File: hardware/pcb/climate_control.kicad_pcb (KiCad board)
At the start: 2 copper layers, 18 x 60 mm, 43 parts, among them J1 Switch, J2 BatteryIn, J3 USB_C, J4 HeatElement, J5 ICSP, Q1 NTR3C21NZ, Q2 NTR3C21NZ, U1 TP4056, U2 XB8089A, U3 ATmega328PB-AU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

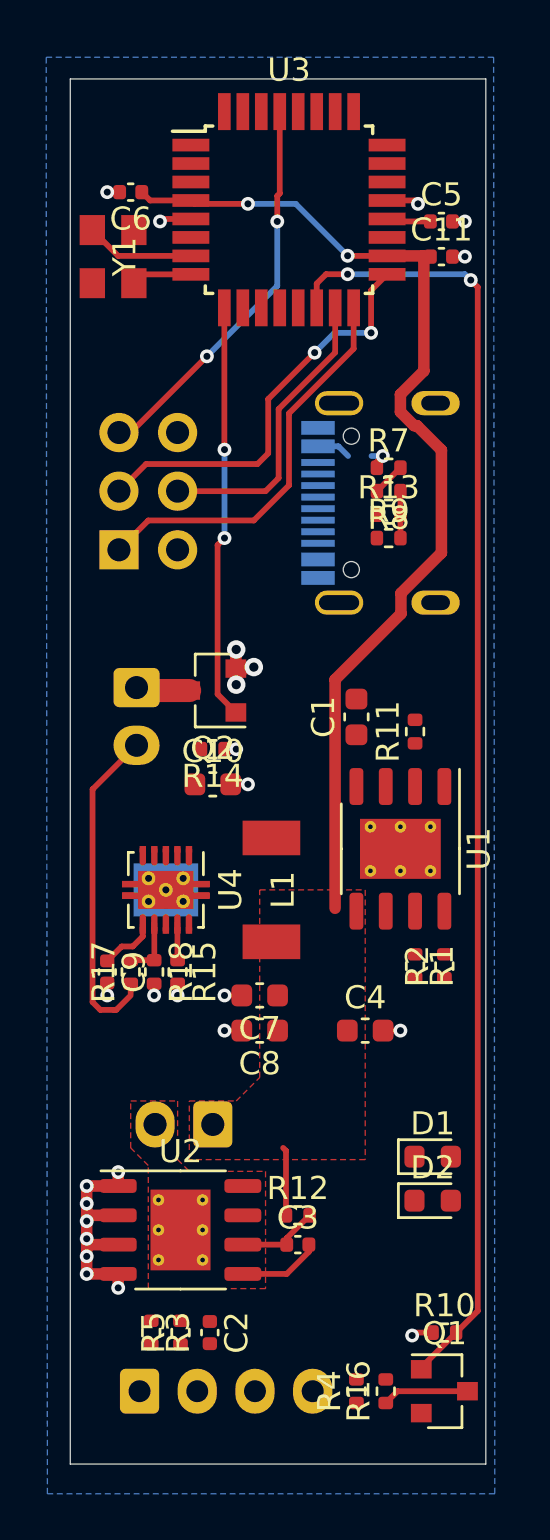
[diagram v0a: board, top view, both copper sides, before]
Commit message: Removed resistor on TP4056.
Updated on PCB the routing.
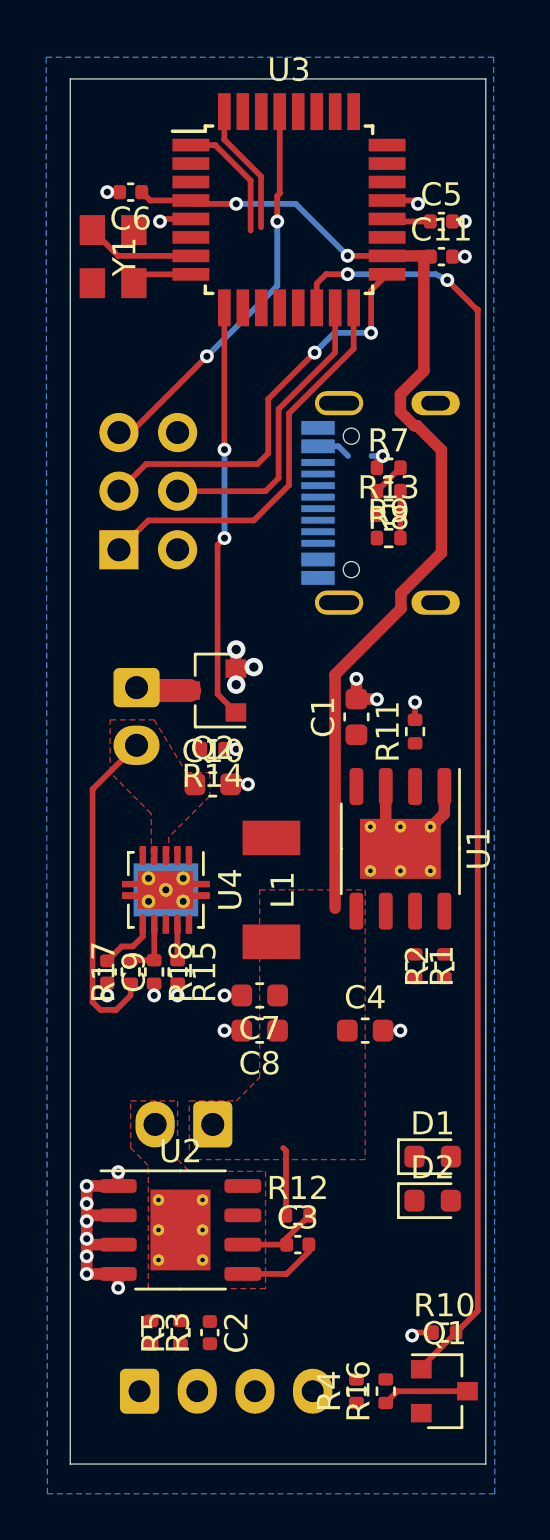
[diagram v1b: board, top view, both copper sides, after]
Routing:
- net GND: track 25.2 -> 34.4 mm, vias 25 -> 28
- net SWITCH: track 0.00 -> 5.67 mm
- net BOOST_EN: track 1.57 -> 6.96 mm
- net LED: track 56.4 -> 55.8 mm
- added copper zone on F.Cu, net +VSW
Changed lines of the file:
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@@
     (thickness 1.6)
     (drawings 4)
-    (tracks 184)
+    (tracks 203)
     (zones 0)
     (modules 43)
@@
   (segment (start 110.335 150.805) (end 109.375 151.765) (width 0.25) (layer F.Cu) (net 1))
   (segment (start 110.335 150.495) (end 110.335 150.805) (width 0.25) (layer F.Cu) (net 1))
+  (segment (start 106.674 102.62759) (end 108.263011 104.216601) (width 0.25) (layer F.Cu) (net 3))
+  (segment (start 106.674 101.414) (end 106.674 102.62759) (width 0.25) (layer F.Cu) (net 3))
+  (segment (start 108.263011 104.216601) (end 108.263011 106.426) (width 0.25) (layer F.Cu) (net 3))
   (segment (start 107.475 150.495) (end 109.375 150.495) (width 0.25) (layer F.Cu) (net 4))
   (segment (start 109.375 150.215) (end 110.365 149.225) (width 0.25) (layer F.Cu) (net 4))
@@
   (via (at 112.014 107.657997) (size 0.6) (drill 0.3) (layers F.Cu B.Cu) (net 5))
   (segment (start 112.020003 107.664) (end 112.014 107.657997) (width 0.25) (layer F.Cu) (net 5))
-  (via (at 107.696 105.41) (size 0.6) (drill 0.3) (layers F.Cu B.Cu) (net 5))
-  (segment (start 112.014 107.657997) (end 109.766003 105.41) (width 0.25) (layer B.Cu) (net 5))
-  (segment (start 109.766003 105.41) (end 107.696 105.41) (width 0.25) (layer B.Cu) (net 5))
-  (segment (start 105.37 105.41) (end 105.224 105.264) (width 0.25) (layer F.Cu) (net 5))
-  (segment (start 107.696 105.41) (end 105.37 105.41) (width 0.25) (layer F.Cu) (net 5))
   (segment (start 109.345 149.225) (end 109.345 146.429) (width 0.25) (layer F.Cu) (net 5))
   (segment (start 109.345 146.429) (end 109.22 146.304) (width 0.25) (layer F.Cu) (net 5))
@@
   (segment (start 103.458 105.264) (end 103.096 104.902) (width 0.25) (layer F.Cu) (net 5))
   (segment (start 105.224 105.264) (end 103.458 105.264) (width 0.25) (layer F.Cu) (net 5))
-  (segment (start 114.32399 123.16601) (end 111.46999 126.02001) (width 0.5) (layer F.Cu) (net 5))
   (segment (start 116.078 116.078) (end 116.078 120.526128) (width 0.5) (layer F.Cu) (net 5))
   (segment (start 116.078 120.526128) (end 114.32399 122.280138) (width 0.5) (layer F.Cu) (net 5))
-  (segment (start 111.46999 126.02001) (end 111.46999 135.92601) (width 0.5) (layer F.Cu) (net 5))
   (segment (start 115.284 107.758002) (end 115.316 107.790002) (width 0.5) (layer F.Cu) (net 5))
   (segment (start 115.284 107.664) (end 115.284 107.758002) (width 0.5) (layer F.Cu) (net 5))
   (segment (start 115.316 107.790002) (end 115.316 112.648128) (width 0.5) (layer F.Cu) (net 5))
-  (segment (start 114.32399 122.280138) (end 114.32399 123.16601) (width 0.5) (layer F.Cu) (net 5))
   (segment (start 115.316 112.648128) (end 114.3 113.664128) (width 0.5) (layer F.Cu) (net 5))
   (segment (start 114.3 114.423872) (end 114.3 113.664128) (width 0.5) (layer F.Cu) (net 5))
@@
   (segment (start 115.01901 115.01901) (end 114.895138 115.01901) (width 0.5) (layer F.Cu) (net 5))
   (segment (start 116.078 116.078) (end 115.01901 115.01901) (width 0.5) (layer F.Cu) (net 5))
+  (segment (start 105.37 105.41) (end 105.224 105.264) (width 0.25) (layer F.Cu) (net 5))
+  (segment (start 107.188 105.41) (end 105.37 105.41) (width 0.25) (layer F.Cu) (net 5))
+  (segment (start 109.766003 105.41) (end 112.014 107.657997) (width 0.25) (layer B.Cu) (net 5))
+  (via (at 107.188 105.41) (size 0.6) (drill 0.3) (layers F.Cu B.Cu) (net 5))
+  (segment (start 107.188 105.41) (end 109.766003 105.41) (width 0.25) (layer B.Cu) (net 5))
+  (segment (start 114.32399 122.945008) (end 114.32399 122.280138) (width 0.5) (layer F.Cu) (net 5))
+  (segment (start 111.46999 125.799008) (end 114.32399 122.945008) (width 0.5) (layer F.Cu) (net 5))
+  (segment (start 111.46999 135.92601) (end 111.46999 125.799008) (width 0.5) (layer F.Cu) (net 5))
   (segment (start 113.832 106.172) (end 113.724 106.064) (width 0.25) (layer F.Cu) (net 6))
   (segment (start 115.598 106.172) (end 113.832 106.172) (width 0.25) (layer F.Cu) (net 6))
@@
   (segment (start 110.674 109.914) (end 110.674 108.864) (width 0.25) (layer F.Cu) (net 15))
   (segment (start 110.674 108.864) (end 111.08 108.458) (width 0.25) (layer F.Cu) (net 15))
-  (via (at 117.348 108.712) (size 0.6) (drill 0.3) (layers F.Cu B.Cu) (net 15))
-  (segment (start 112.014 108.458) (end 117.094 108.458) (width 0.25) (layer B.Cu) (net 15))
-  (segment (start 117.094 108.458) (end 117.348 108.712) (width 0.25) (layer B.Cu) (net 15))
-  (segment (start 117.64999 153.37001) (end 116.715 154.305) (width 0.25) (layer F.Cu) (net 15))
-  (segment (start 117.348 108.712) (end 117.64999 109.01399) (width 0.25) (layer F.Cu) (net 15))
-  (segment (start 117.64999 109.01399) (end 117.64999 153.37001) (width 0.25) (layer F.Cu) (net 15))
   (segment (start 115.205 155.815) (end 116.715 154.305) (width 0.25) (layer F.Cu) (net 15))
   (segment (start 115.205 155.895) (end 115.205 155.815) (width 0.25) (layer F.Cu) (net 15))
+  (via (at 116.332 108.712) (size 0.6) (drill 0.3) (layers F.Cu B.Cu) (net 15))
+  (segment (start 115.824 108.458) (end 112.014 108.458) (width 0.25) (layer B.Cu) (net 15))
+  (segment (start 116.332 108.712) (end 115.824 108.458) (width 0.25) (layer B.Cu) (net 15))
+  (segment (start 117.64999 153.37001) (end 116.715 154.305) (width 0.25) (layer F.Cu) (net 15))
+  (segment (start 117.64999 109.982) (end 117.64999 153.37001) (width 0.25) (layer F.Cu) (net 15))
+  (segment (start 117.602 109.982) (end 116.332 108.712) (width 0.25) (layer F.Cu) (net 15))
+  (segment (start 117.64999 109.982) (end 117.602 109.982) (width 0.25) (layer F.Cu) (net 15))
   (via (at 106.68 116.055999) (size 0.6) (drill 0.3) (layers F.Cu B.Cu) (net 18))
   (segment (start 106.674 109.914) (end 106.674 116.049999) (width 0.25) (layer F.Cu) (net 18))
@@
   (segment (start 104.64 138.166) (end 104.648 138.174) (width 0.25) (layer F.Cu) (net 19))
   (segment (start 104.64 136.603) (end 104.64 138.166) (width 0.25) (layer F.Cu) (net 19))
+  (segment (start 107.813001 104.403001) (end 107.813001 106.562999) (width 0.25) (layer F.Cu) (net 19))
+  (segment (start 105.224 102.864) (end 106.274 102.864) (width 0.25) (layer F.Cu) (net 19))
+  (segment (start 106.274 102.864) (end 107.813001 104.403001) (width 0.25) (layer F.Cu) (net 19))
   (segment (start 103.64 138.166) (end 103.632 138.174) (width 0.25) (layer F.Cu) (net 21))
   (segment (start 103.64 136.603) (end 103.64 138.166) (width 0.25) (layer F.Cu) (net 21))
@@
   (segment (start 102.136 104.902) (end 101.6 104.902) (width 0.25) (layer F.Cu) (net 56))
   (segment (start 114.302 117.856) (end 114.302 119.888) (width 0.25) (layer F.Cu) (net 56))
+  (segment (start 113.665 132.715) (end 114.3 133.35) (width 0.5) (layer F.Cu) (net 56))
+  (segment (start 113.665 130.65) (end 113.665 132.715) (width 0.5) (layer F.Cu) (net 56))
+  (segment (start 116.205 130.65) (end 116.205 131.826) (width 0.5) (layer F.Cu) (net 56))
+  (segment (start 114.681 133.35) (end 114.3 133.35) (width 0.5) (layer F.Cu) (net 56))
+  (segment (start 116.205 131.826) (end 114.681 133.35) (width 0.5) (layer F.Cu) (net 56))
+  (via (at 114.935 127) (size 0.6) (drill 0.3) (layers F.Cu B.Cu) (net 56))
+  (segment (start 114.935 127.76) (end 114.935 127) (width 0.25) (layer F.Cu) (net 56))
+  (via (at 113.284 126.873) (size 0.6) (drill 0.3) (layers F.Cu B.Cu) (net 56))
+  (segment (start 112.395 126.86) (end 113.271 126.86) (width 0.5) (layer F.Cu) (net 56))
+  (segment (start 113.271 126.86) (end 113.284 126.873) (width 0.5) (layer F.Cu) (net 56))
+  (segment (start 112.395 126.86) (end 112.395 125.984) (width 0.5) (layer F.Cu) (net 56))
+  (via (at 112.395 125.984) (size 0.6) (drill 0.3) (layers F.Cu B.Cu) (net 56))
   (zone (net 56) (net_name GND) (layer B.Cu) (hatch edge 0.508)
     (connect_pads (clearance 0.508))
@@
       )
     )
+  )
+  (zone (net 8) (net_name +VSW) (layer F.Cu) (hatch edge 0.508)
+    (connect_pads (clearance 0.508))
+    (min_thickness 0.254)
+    (fill yes (arc_segments 32) (thermal_gap 0.508) (thermal_bridge_width 0.508))
+    (polygon
+      (pts
+        (xy 105.029 130.048) (xy 106.045 130.048) (xy 106.045 131.064) (xy 104.267 132.842) (xy 104.267 133.985)
+        (xy 103.505 133.985) (xy 103.505 131.826) (xy 101.727 130.048) (xy 101.727 127.762) (xy 103.632 127.762)
+      )
+    )

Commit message: First routing complete.
The first routing is done, now it must be improved!
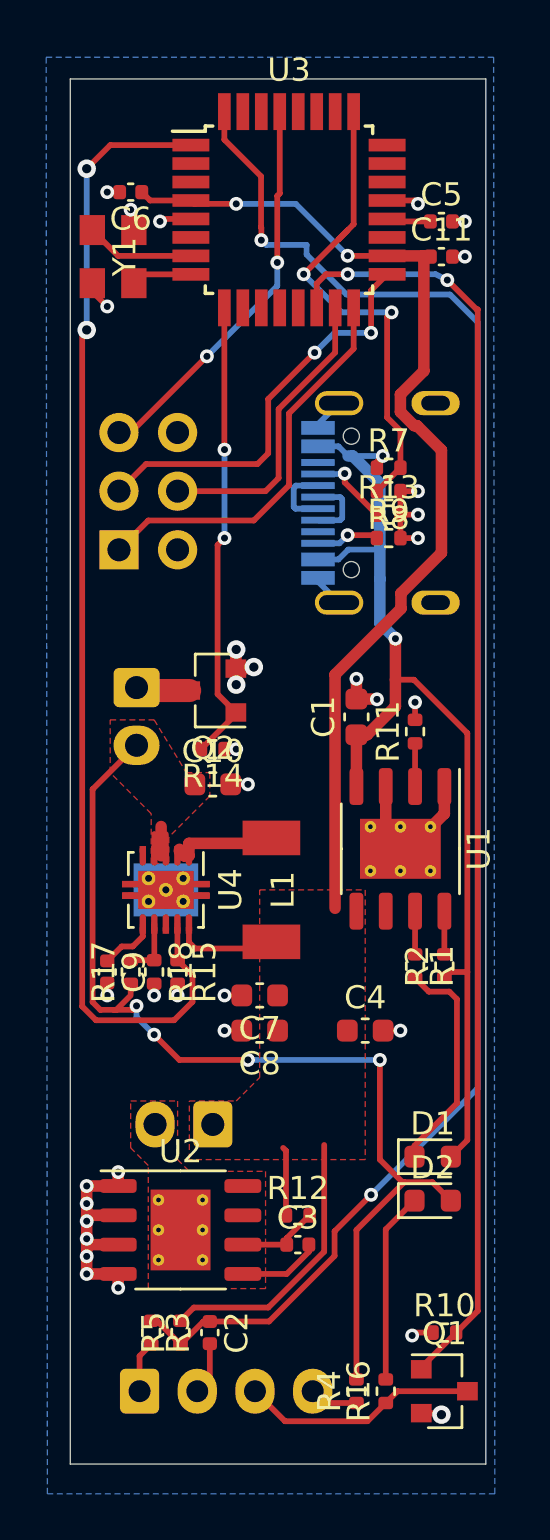
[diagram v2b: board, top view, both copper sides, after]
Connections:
- C1 pad 1: Net-(C1-Pad1) -> +5V
- D1 pad 2: Net-(C1-Pad1) -> +5V
- R2 pad 1: Net-(C1-Pad1) -> +5V
- U1 pad 4: Net-(C1-Pad1) -> +5V
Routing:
- net SWITCH: track 5.67 -> 70.3 mm, vias 0 -> 2
- net +5V: track 2.58 -> 46.6 mm, vias 1 -> 2
- net BOOST_EN: track 6.96 -> 50.3 mm, vias 0 -> 2
- net +VSW: track 14.4 -> 48.3 mm, vias 0 -> 4
- net USB_DET: track 1.44 -> 21.5 mm, vias 0 -> 2
- net +BATT: track 48.0 -> 64.7 mm
- net GND: track 34.4 -> 50.6 mm, vias 28 -> 34
- net Net-(D1-Pad1): track 0.00 -> 9.78 mm
- net Net-(D2-Pad1): track 0.00 -> 8.26 mm
- net Net-(J1-Pad3): track 3.75 -> 10.3 mm
- net Net-(L1-Pad2): track 0.00 -> 4.79 mm
- net Net-(J3-PadA5): track 0.00 -> 3.52 mm, vias 0 -> 1
- net USB_D-: track 0.00 -> 3.00 mm
- net USB_D+: track 0.00 -> 2.99 mm
- net Net-(J3-PadB5): track 0.00 -> 2.75 mm, vias 0 -> 1
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
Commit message: Removed unnececary components
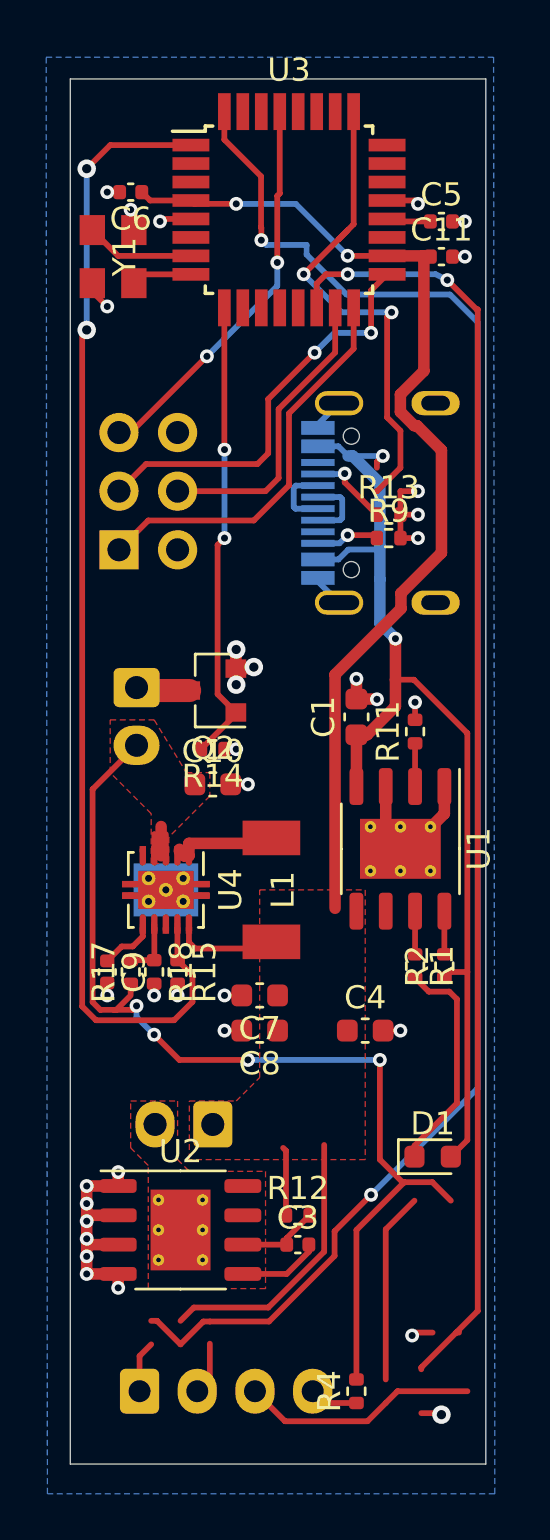
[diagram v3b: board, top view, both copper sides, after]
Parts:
- removed C2: 100nF, Capacitor_SMD:C_0402_1005Metric
- removed D2: STAT, Diode_SMD:D_0603_1608Metric
- removed Q1: NTR3C21NZ, Package_TO_SOT_SMD:SOT-23
- removed R10, R5, R8: 10k, Resistor_SMD:R_0402_1005Metric
- removed R16: x, Resistor_SMD:R_0402_1005Metric
- removed R3, R7: 1k, Resistor_SMD:R_0402_1005Metric
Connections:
- J1 pad 1: Net-(J1-Pad1) -> SWITCH
- J1 pad 3: Net-(J1-Pad3) -> LED
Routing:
- net Net-(J1-Pad3): track 10.3 -> 0.00 mm
- net LED: track 55.8 -> 66.1 mm
- net Net-(J1-Pad1): track 2.24 -> 0.00 mm
- net SWITCH: track 70.3 -> 72.5 mm

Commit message: Second routing process done
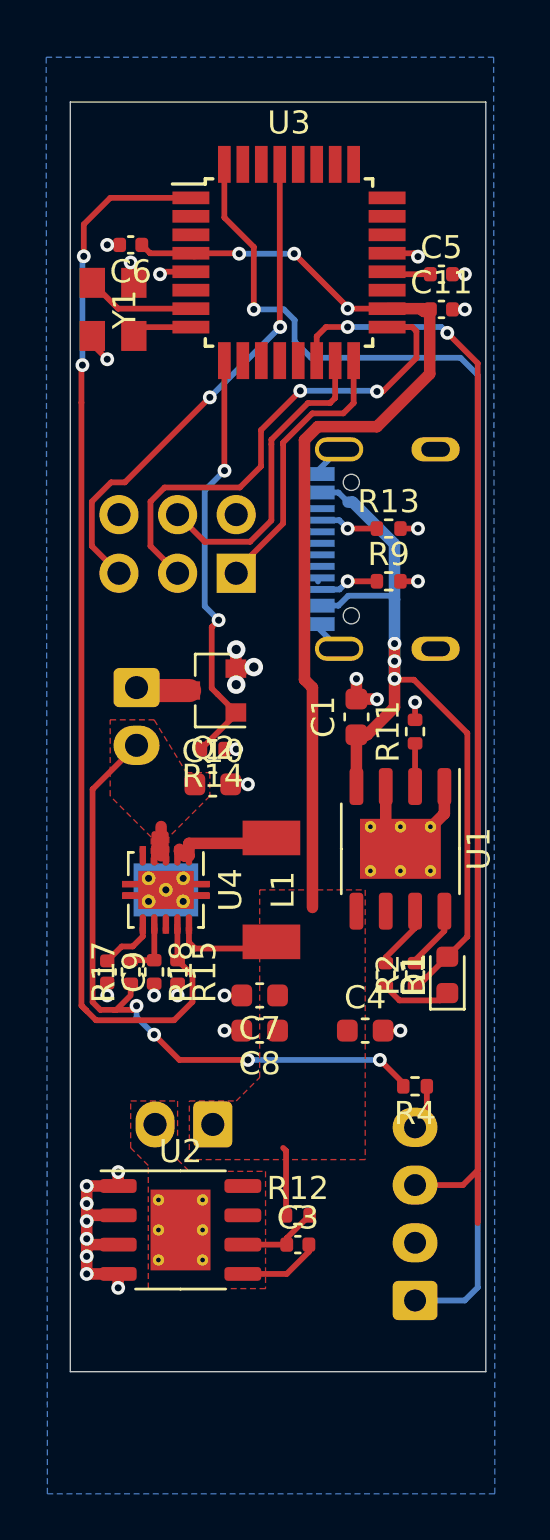
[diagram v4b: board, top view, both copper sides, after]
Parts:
- moved R4 13.5 mm to (114.9, 143.6), turned to 180 degrees
- moved J1 12.6 mm to (114.9, 152.9), turned to 90 degrees
- moved D1 7.90 mm to (116.3, 138.8), turned to 90 degrees
- moved J5 5.18 mm to (107.2, 121.4), turned to 90 degrees
- moved C11 2.29 mm to (116.1, 110.0)
- moved C5 2.29 mm to (116.1, 108.5)
- moved C6 2.29 mm to (102.6, 107.2)
- moved U3 2.29 mm to (109.5, 108.0)
- moved Y1 2.29 mm to (101.9, 110.0)
- moved J3 2.00 mm to (115.8, 120.4)
- moved R9 1.87 mm to (113.8, 121.8)
- moved R1 1.33 mm to (113.7, 138.8)
- moved R2 1.33 mm to (114.9, 138.8)
- moved R13 0.60 mm to (113.8, 119.5)
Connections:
- J3 pad A6: USB_D+ -> Net-(J3-PadA6)
- J3 pad A7: USB_D- -> Net-(J3-PadA7)
- J3 pad B6: USB_D+ -> Net-(J3-PadB6)
- J3 pad B7: USB_D- -> Net-(J3-PadB7)
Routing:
- net USB_DET: track 21.5 -> 0.00 mm, vias 2 -> 0
- net LED: track 66.1 -> 49.1 mm
- net +VSW: track 48.3 -> 32.3 mm
- net +BATT: track 64.7 -> 51.4 mm, vias 2 -> 3
- net SWITCH: track 72.5 -> 60.7 mm, vias 2 -> 1
- net +5V: track 46.6 -> 36.9 mm, vias 2 -> 3
- net Net-(D2-Pad1): track 8.26 -> 0.00 mm
- net GND: track 50.6 -> 43.4 mm, vias 34 -> 31
- net Net-(D1-Pad1): track 9.78 -> 3.04 mm
- net MISO: track 17.4 -> 12.1 mm
- net ~RST: track 17.1 -> 21.9 mm
- net SCK: track 18.0 -> 21.1 mm
- net USB_D-: track 3.00 -> 0.00 mm
- net USB_D+: track 2.99 -> 0.00 mm
- net BOOST_EN: track 50.3 -> 48.3 mm
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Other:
- board size 18 x 60 mm -> 18 x 55 mm
- board text added: "-|MOSI|GND"
- board text added: "B+"
- board text added: "B-"
- board text added: "GND"
- board text added: "H+"
- board text added: "H-"
- board text added: "L+"
- board text added: "L-"
- board text added: "MISO|SCK|RST"
- board text added: "SW"
